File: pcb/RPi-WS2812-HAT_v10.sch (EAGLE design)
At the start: 104 parts, among them IC1 24LC-I/OT, IC2 ATTINY85-MU, J1 USB-MICRO, X1 PASSER-07, X2 PASSER-07, X3 PASSER-07

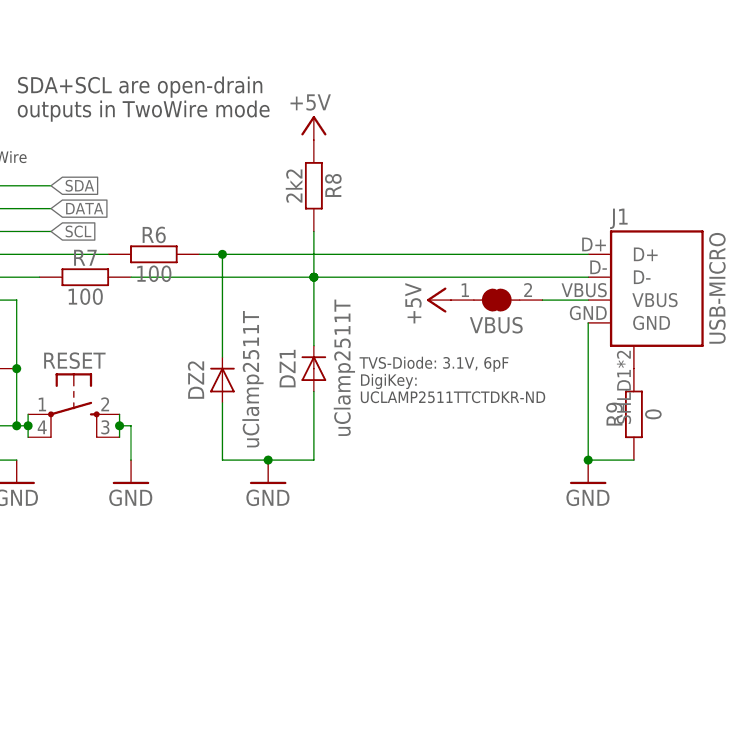
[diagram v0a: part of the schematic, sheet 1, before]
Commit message: updated schematics
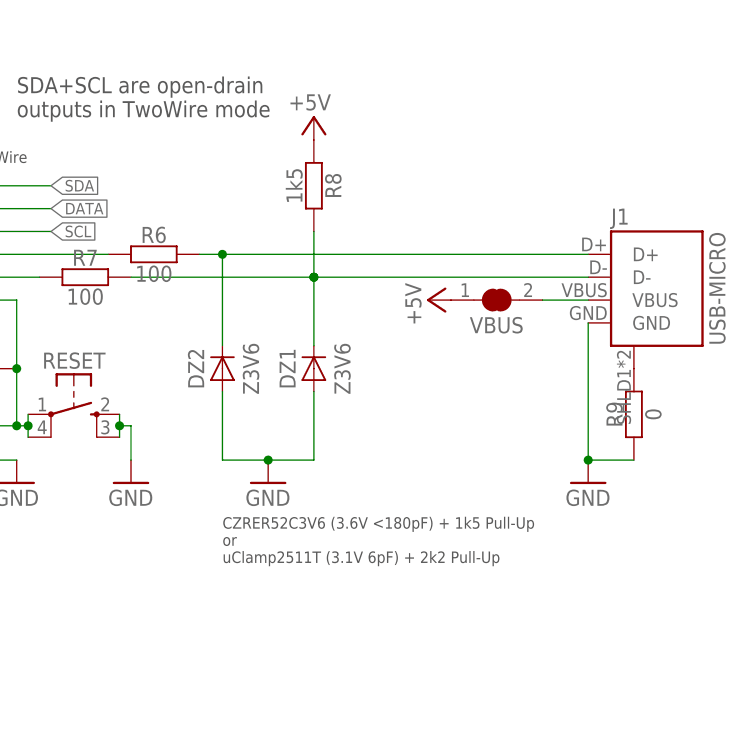
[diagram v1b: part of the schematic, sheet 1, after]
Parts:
- DZ1, DZ2: value uClamp2511T -> Z3V6
- R8: value 2k2 -> 1k5
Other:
- note added: "CZRER52C3V6 (3.6V <180pF) + 1k5 Pull-Up or uClamp2511T (3.1V 6pF) + 2k2 Pull-Up"
- note removed: "TVS-Diode: 3.1V, 6pF DigiKey: UCLAMP2511TTCTDKR-ND"
- moved on the sheet: DZ2
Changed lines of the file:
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@@
 <part name="GND19" library="supply1" deviceset="GND" device=""/>
 <part name="DAT" library="we-rcl" deviceset="JUMPER3" device="-0603"/>
-<part name="R8" library="we-rcl" deviceset="RESISTOR" device="-R0402" value="2k2"/>
+<part name="R8" library="we-rcl" deviceset="RESISTOR" device="-R0402" value="1k5"/>
 <part name="RESET" library="we-switch" deviceset="SW-TACTILE" device="-TL3315"/>
 <part name="GND20" library="supply1" deviceset="GND" device=""/>
@@
 <part name="P+16" library="supply1" deviceset="+5V" device=""/>
 <part name="P+17" library="supply1" deviceset="+5V" device=""/>
-<part name="DZ1" library="we-rcl" deviceset="DIODE" device="-SOD882" value="uClamp2511T"/>
-<part name="DZ2" library="we-rcl" deviceset="DIODE" device="-SOD882" value="uClamp2511T"/>
+<part name="DZ1" library="we-rcl" deviceset="DIODE" device="-SOD882" value="Z3V6"/>
+<part name="DZ2" library="we-rcl" deviceset="DIODE" device="-SOD882" value="Z3V6"/>
 <part name="GND15" library="supply1" deviceset="GND" device=""/>
 <part name="P+10" library="supply1" deviceset="+5V" device=""/>
@@
 <text x="91.44" y="93.98" size="1.778" layer="97">The used USB-Bootloader on the ATtiny85 is Micronucleus
 https://github.com/micronucleus/micronucleus</text>
-<text x="203.2" y="62.23" size="1.27" layer="97">TVS-Diode: 3.1V, 6pF
-DigiKey:
-UCLAMP2511TTCTDKR-ND</text>
+<text x="187.96" y="44.45" size="1.27" layer="97">CZRER52C3V6 (3.6V &lt;180pF) + 1k5 Pull-Up
+or
+uClamp2511T (3.1V 6pF) + 2k2 Pull-Up</text>
 <text x="158.75" y="83.82" size="1.27" layer="97">Pin 1</text>
 <text x="158.75" y="86.36" size="1.27" layer="97">Pin 4</text>
@@
 </instance>
 <instance part="DZ1" gate="D" x="198.12" y="66.04" rot="R90"/>
-<instance part="DZ2" gate="D" x="187.96" y="64.77" rot="R90"/>
+<instance part="DZ2" gate="D" x="187.96" y="66.04" rot="R90"/>
 <instance part="GND15" gate="1" x="193.04" y="53.34" smashed="yes">
 <attribute name="VALUE" x="190.5" y="50.8" size="1.778" layer="96"/>
@@
 <wire x1="198.12" y1="55.88" x2="193.04" y2="55.88" width="0.1524" layer="91"/>
 <pinref part="DZ2" gate="D" pin="A"/>
-<wire x1="187.96" y1="62.23" x2="187.96" y2="55.88" width="0.1524" layer="91"/>
+<wire x1="187.96" y1="63.5" x2="187.96" y2="55.88" width="0.1524" layer="91"/>
 <wire x1="187.96" y1="55.88" x2="193.04" y2="55.88" width="0.1524" layer="91"/>
 <junction x="193.04" y="55.88"/>
@@
 <pinref part="DZ2" gate="D" pin="C"/>
 <wire x1="187.96" y1="78.74" x2="228.6" y2="78.74" width="0.1524" layer="91"/>
-<wire x1="187.96" y1="78.74" x2="187.96" y2="67.31" width="0.1524" layer="91"/>
+<wire x1="187.96" y1="78.74" x2="187.96" y2="68.58" width="0.1524" layer="91"/>
 <junction x="187.96" y="78.74"/>
 </segment>
